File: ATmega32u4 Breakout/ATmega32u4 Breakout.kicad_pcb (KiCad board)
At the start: 2 copper layers, 6 parts, among them J1 Conn_01x22_Male, J2 Conn_01x22_Male, U1 ATmega32U4-AU, Y1 16MHz

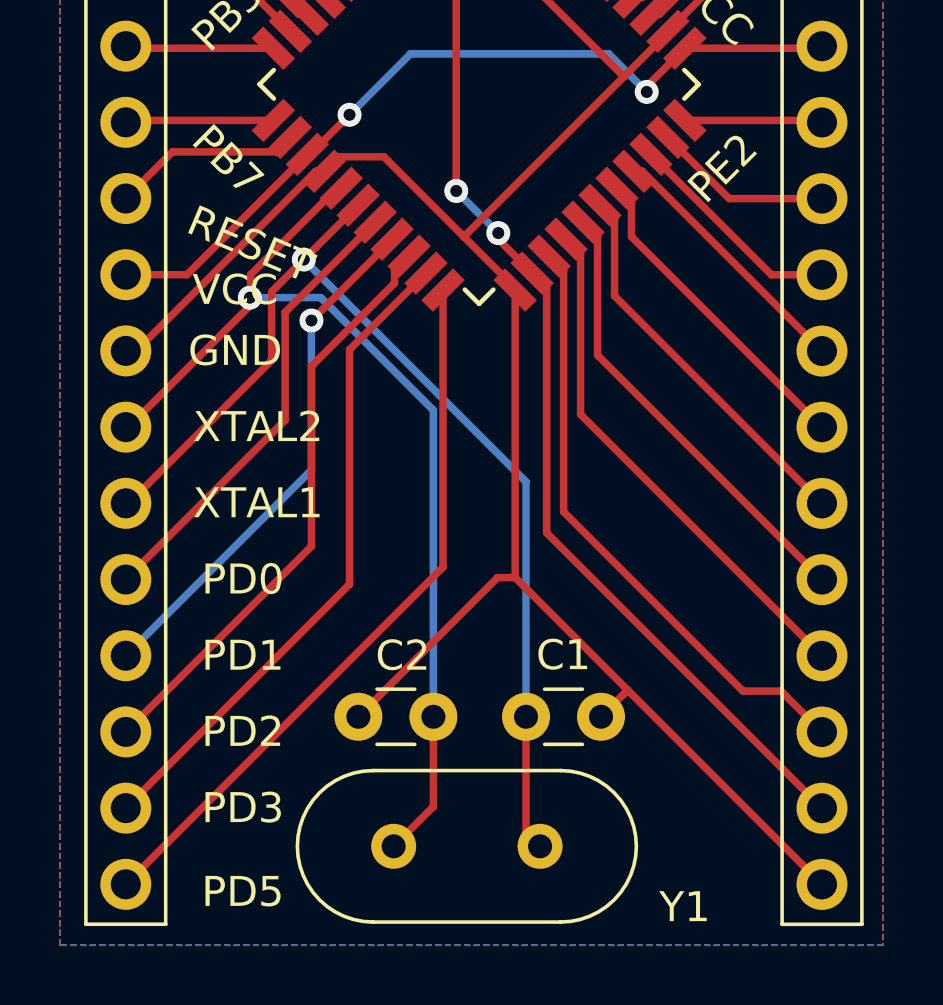
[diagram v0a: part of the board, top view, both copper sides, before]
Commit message: Moving labels around
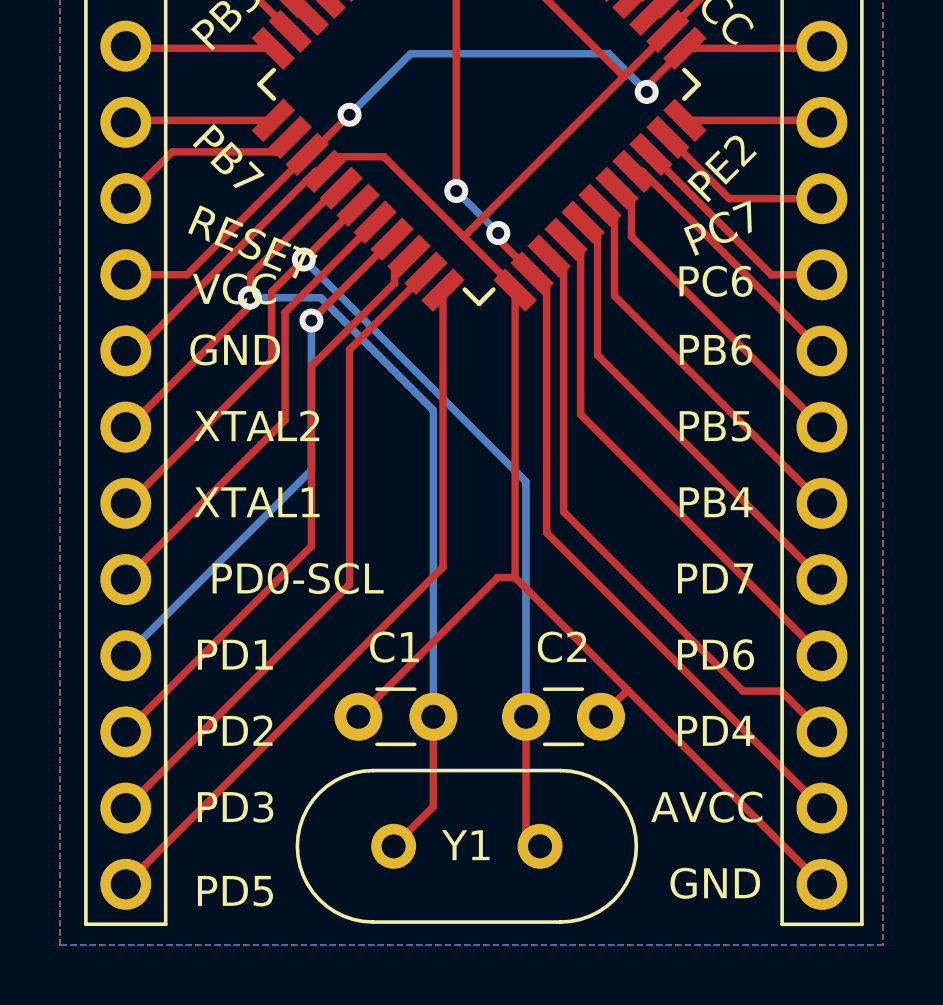
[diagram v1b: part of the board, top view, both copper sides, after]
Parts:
- moved C1 3.09 mm to (154.2, 110.0), turned to 180 degrees
- moved C2 3.09 mm to (157.3, 110.0), turned to 0 degrees
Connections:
- C1 pad 1: XTAL1 -> XTAL2
- C2 pad 1: XTAL2 -> XTAL1
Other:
- board text added: "PB4"
- board text added: "PB5"
- board text added: "PB6"
- board text added: "PC6"
- board text added: "PC7"
- board text added: "PD0-SCL"
- board text added: "PD4"
- board text added: "PD6"
- board text added: "PD7"
- board text removed: "PD0"
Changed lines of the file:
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@@
   (general
     (thickness 1.6)
-    (drawings 38)
+    (drawings 48)
     (tracks 180)
     (zones 0)
@@
   (page A4)
   (layers
-    (0 F.Cu signal)
+    (0 F.Cu signal hide)
     (31 B.Cu signal)
     (32 B.Adhes user)
@@
     (descr "C, Disc series, Radial, pin pitch=2.50mm, , diameter*width=3.0*1.6mm^2, Capacitor, http://www.vishay.com/docs/45233/krseries.pdf")
     (tags "C Disc series Radial pin pitch 2.50mm  diameter 3.0mm width 1.6mm Capacitor")
-    (fp_text reference C1 (at 1.25 -2.05) (layer F.SilkS)
-      (effects (font (size 1 1) (thickness 0.15)))
-    )
-    (fp_text value 22pF (at 5.548 0) (layer F.Fab)
+    (fp_text reference C2 (at 1.23 -2.286) (layer F.SilkS)
+      (effects (font (size 1 1) (thickness 0.15)))
+    )
+    (fp_text value 22pF (at 1.484 -2.286) (layer F.Fab)
       (effects (font (size 1 1) (thickness 0.15)))
     )
@@
     (descr "C, Disc series, Radial, pin pitch=2.50mm, , diameter*width=3.0*1.6mm^2, Capacitor, http://www.vishay.com/docs/45233/krseries.pdf")
     (tags "C Disc series Radial pin pitch 2.50mm  diameter 3.0mm width 1.6mm Capacitor")
-    (fp_text reference C2 (at 1.016 2.032) (layer F.SilkS)
-      (effects (font (size 1 1) (thickness 0.15)))
-    )
-    (fp_text value 22pF (at 5.588 0) (layer F.Fab)
+    (fp_text reference C1 (at 1.27 2.286) (layer F.SilkS)
+      (effects (font (size 1 1) (thickness 0.15)))
+    )
+    (fp_text value 22pF (at 1.016 2.286) (layer F.Fab)
       (effects (font (size 1 1) (thickness 0.15)))
     )
@@
     (descr "Crystal THT HC-49/U http://5hertz.com/pdfs/04404_D.pdf")
     (tags "THT crystalHC-49/U")
-    (fp_text reference Y1 (at -4.826 -2.032) (layer F.SilkS)
+    (fp_text reference Y1 (at 2.413 0) (layer F.SilkS)
       (effects (font (size 1 1) (thickness 0.15)))
     )
@@
     )
   )
+  (gr_text GND (at 163.576 115.57) (layer F.SilkS)
+    (effects (font (size 1 1) (thickness 0.15)))
+  )
+  (gr_text AVCC (at 163.322 113.03) (layer F.SilkS)
+    (effects (font (size 1 1) (thickness 0.15)))
+  )
+  (gr_text PD4 (at 163.576 110.49) (layer F.SilkS)
+    (effects (font (size 1 1) (thickness 0.15)))
+  )
+  (gr_text PD6 (at 163.576 107.95) (layer F.SilkS)
+    (effects (font (size 1 1) (thickness 0.15)))
+  )
+  (gr_text PD7 (at 163.576 105.41) (layer F.SilkS)
+    (effects (font (size 1 1) (thickness 0.15)))
+  )
+  (gr_text PB4 (at 163.576 102.87) (layer F.SilkS)
+    (effects (font (size 1 1) (thickness 0.15)))
+  )
+  (gr_text PB5 (at 163.576 100.33) (layer F.SilkS)
+    (effects (font (size 1 1) (thickness 0.15)))
+  )
+  (gr_text PB6 (at 163.576 97.79) (layer F.SilkS)
+    (effects (font (size 1 1) (thickness 0.15)))
+  )
+  (gr_text PC6 (at 163.576 95.504) (layer F.SilkS)
+    (effects (font (size 1 1) (thickness 0.15)))
+  )
+  (gr_text PC7 (at 163.83 93.726 23) (layer F.SilkS)
+    (effects (font (size 1 1) (thickness 0.15)))
+  )
   (gr_text PE2 (at 163.83 91.694 45) (layer F.SilkS)
     (effects (font (size 1 1) (thickness 0.15)))
@@
     (effects (font (size 1 1) (thickness 0.15)))
   )
-  (gr_text PD5 (at 147.828 115.824) (layer F.SilkS)
-    (effects (font (size 1 1) (thickness 0.15)))
-  )
-  (gr_text PD3 (at 147.828 113.03) (layer F.SilkS)
-    (effects (font (size 1 1) (thickness 0.15)))
-  )
-  (gr_text PD2 (at 147.828 110.49) (layer F.SilkS)
-    (effects (font (size 1 1) (thickness 0.15)))
-  )
-  (gr_text PD1 (at 147.828 107.95) (layer F.SilkS)
-    (effects (font (size 1 1) (thickness 0.15)))
-  )
-  (gr_text PD0 (at 147.828 105.41) (layer F.SilkS)
+  (gr_text PD5 (at 147.574 115.824) (layer F.SilkS)
+    (effects (font (size 1 1) (thickness 0.15)))
+  )
+  (gr_text PD3 (at 147.574 113.03) (layer F.SilkS)
+    (effects (font (size 1 1) (thickness 0.15)))
+  )
+  (gr_text PD2 (at 147.574 110.49) (layer F.SilkS)
+    (effects (font (size 1 1) (thickness 0.15)))
+  )
+  (gr_text PD1 (at 147.574 107.95) (layer F.SilkS)
+    (effects (font (size 1 1) (thickness 0.15)))
+  )
+  (gr_text PD0-SCL (at 149.606 105.41) (layer F.SilkS)
     (effects (font (size 1 1) (thickness 0.15)))
   )
@@
   (segment (start 160.528 88.646) (end 155.194 93.98) (width 0.25) (layer F.Cu) (net 15))
   (segment (start 161.99525 87.17875) (end 160.528 88.646) (width 0.25) (layer F.Cu) (net 15) (status 10))
-  (segment (start 159.766 109.982) (end 160.528 109.22) (width 0.25) (layer F.Cu) (net 15))
+  (segment (start 159.766 109.982) (end 160.528 109.22) (width 0.25) (layer F.Cu) (net 15) (status 10))
   (segment (start 160.528 109.22) (end 160.655 109.093) (width 0.25) (layer F.Cu) (net 15))
-  (segment (start 160.655 109.093) (end 167.132 115.57) (width 0.25) (layer F.Cu) (net 15))
+  (segment (start 160.655 109.093) (end 167.132 115.57) (width 0.25) (layer F.Cu) (net 15) (status 20))
   (segment (start 156.904082 105.342082) (end 160.655 109.093) (width 0.25) (layer F.Cu) (net 15))
   (segment (start 156.317918 105.342082) (end 156.904082 105.342082) (width 0.25) (layer F.Cu) (net 15))
-  (segment (start 151.678 109.982) (end 156.317918 105.342082) (width 0.25) (layer F.Cu) (net 15))
+  (segment (start 151.678 109.982) (end 156.317918 105.342082) (width 0.25) (layer F.Cu) (net 15) (status 10))
   (segment (start 150.851806 92.480194) (end 148.082 95.25) (width 0.25) (layer F.Cu) (net 16) (status 10))
   (segment (start 148.082 95.25) (end 148.082 96.127371) (width 0.25) (layer F.Cu) (net 16))
   (segment (start 144.020999 100.327001) (end 143.925001 100.327001) (width 0.25) (layer F.Cu) (net 16) (status 30))
   (segment (start 148.336 96.012) (end 144.020999 100.327001) (width 0.25) (layer F.Cu) (net 16) (status 20))
-  (segment (start 154.178 112.976) (end 152.854 114.3) (width 0.25) (layer F.Cu) (net 16))
-  (segment (start 154.178 109.982) (end 154.178 112.976) (width 0.25) (layer F.Cu) (net 16))
+  (segment (start 154.178 112.976) (end 152.854 114.3) (width 0.25) (layer F.Cu) (net 16) (status 20))
+  (segment (start 154.178 109.982) (end 154.178 112.976) (width 0.25) (layer F.Cu) (net 16) (status 10))
   (via (at 148.06101 96.012) (size 0.8) (drill 0.4) (layers F.Cu B.Cu) (net 16))
   (segment (start 150.425002 96.012) (end 148.06101 96.012) (width 0.25) (layer B.Cu) (net 16))
   (segment (start 154.178 99.764998) (end 150.425002 96.012) (width 0.25) (layer B.Cu) (net 16))
-  (segment (start 154.178 109.982) (end 154.178 99.764998) (width 0.25) (layer B.Cu) (net 16))
+  (segment (start 154.178 109.982) (end 154.178 99.764998) (width 0.25) (layer B.Cu) (net 16) (status 10))
   (segment (start 148.78601 95.81599) (end 148.78601 98.10199) (width 0.25) (layer F.Cu) (net 17))
   (segment (start 144.020999 102.867001) (end 143.925001 102.867001) (width 0.25) (layer F.Cu) (net 17) (status 30))
   (segment (start 148.78601 98.10199) (end 144.020999 102.867001) (width 0.25) (layer F.Cu) (net 17) (status 20))
-  (segment (start 157.266 113.832) (end 157.734 114.3) (width 0.25) (layer F.Cu) (net 17))
-  (segment (start 157.266 109.982) (end 157.266 113.832) (width 0.25) (layer F.Cu) (net 17))
-  (via (at 157.266 109.982) (size 0.8) (drill 0.4) (layers F.Cu B.Cu) (net 17))
+  (segment (start 157.266 113.832) (end 157.734 114.3) (width 0.25) (layer F.Cu) (net 17) (status 30))
+  (segment (start 157.266 109.982) (end 157.266 113.832) (width 0.25) (layer F.Cu) (net 17) (status 30))
+  (via (at 157.266 109.982) (size 0.8) (drill 0.4) (layers F.Cu B.Cu) (net 17) (status 30))
   (segment (start 157.266 102.148) (end 149.86 94.742) (width 0.25) (layer B.Cu) (net 17))
   (via (at 149.86 94.742) (size 0.8) (drill 0.4) (layers F.Cu B.Cu) (net 17))
-  (segment (start 157.266 109.982) (end 157.266 102.148) (width 0.25) (layer B.Cu) (net 17))
+  (segment (start 157.266 109.982) (end 157.266 102.148) (width 0.25) (layer B.Cu) (net 17) (status 10))
   (segment (start 149.86 94.742) (end 148.78601 95.81599) (width 0.25) (layer F.Cu) (net 17))
-  (segment (start 151.671491 92.930509) (end 149.86 94.742) (width 0.25) (layer F.Cu) (net 17))
+  (segment (start 151.671491 92.930509) (end 149.86 94.742) (width 0.25) (layer F.Cu) (net 17) (status 10))
   (segment (start 149.236019 100.095983) (end 143.925001 105.407001) (width 0.25) (layer F.Cu) (net 18) (status 20))
   (segment (start 149.236019 96.497352) (end 149.236019 100.095983) (width 0.25) (layer F.Cu) (net 18))
@@
   (segment (start 159.944643 84.869491) (end 161.777067 83.037067) (width 0.25) (layer F.Cu) (net 35) (status 10))
   (segment (start 159.732509 84.869491) (end 159.944643 84.869491) (width 0.25) (layer F.Cu) (net 35) (status 30))
-  (segment (start 161.777067 80.284933) (end 167.132 74.93) (width 0.25) (layer F.Cu) (net 35))
+  (segment (start 161.777067 80.284933) (end 167.132 74.93) (width 0.25) (layer F.Cu) (net 35) (status 20))
   (segment (start 161.777067 83.037067) (end 161.777067 80.284933) (width 0.25) (layer F.Cu) (net 35))
   (segment (start 159.166823 84.303806) (end 161.036 82.434629) (width 0.25) (layer F.Cu) (net 36) (status 10))

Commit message: Lots of work over the weekend.
Nearly done, gerber files made too.  I think it's ready to be turned into PCB.
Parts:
- moved J2 17.4 mm to (152.1, 71.1)
- moved U1 16.3 mm to (142.0, 97.8)
- moved Y1 16.1 mm to (142.0, 117.6), turned to 270 degrees
- moved J1 15.0 mm to (131.8, 71.1)
- moved C2 14.3 mm to (143.3, 112.8), turned to 90 degrees
- moved C1 13.5 mm to (140.7, 110.2), turned to 270 degrees
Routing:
- net GND: track 95.5 -> 76.7 mm
- net XTAL1: track 36.0 -> 31.4 mm, vias 2 -> 1
- net VCC: track 27.5 -> 23.5 mm
- net PB1: track 7.71 -> 5.97 mm
- net PB3: track 4.95 -> 3.33 mm
- net PB7: track 4.94 -> 3.33 mm
- net PE2: track 4.60 -> 3.08 mm
- net PB2: track 6.33 -> 4.97 mm
- net PD4: track 20.4 -> 19.1 mm
- net PC7: track 5.98 -> 4.71 mm
- net PC6: track 7.37 -> 6.10 mm
- net PF4: track 13.8 -> 12.6 mm
- net PF7: track 7.37 -> 6.26 mm
- net PB0: track 9.10 -> 8.06 mm
- net AREF: track 20.1 -> 19.1 mm
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- removed copper zone on F.Cu, net GND
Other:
- board outline added: 24.4 x 57.4 mm
- net class Power added: clearance 0.2, trace_width 0.4, via_dia 0.7, via_drill 0.5
- rule pad_to_mask_clearance: 0 -> 0.0508
- board text added: "ATmega32u4"
- board text added: "PB0-SS"
- board text added: "PB1-SCLK"
- board text added: "PB2-MOSI"
- board text added: "PB3-MISO"
- board text added: "PB4-A11"
- board text added: "PB5-A12"
- board text added: "PB6-A10"
- board text added: "PD1-SDA"
- board text added: "PD2-RXD"
- board text added: "PD3-TXD"
- board text added: "PD6-T1"
- board text added: "PD7-T0"
- board text added: "PE6-D7"
- board text added: "PF0-A0"
- board text added: "PF1-A1"
- board text added: "PF4-A4"
- board text added: "PF5-A5"
- board text added: "PF6-A6"
- board text added: "PF7-A7"
- board text added: "RES"
- board text added: "SRT0001"
- board text removed: "D7"
- board text removed: "PB0"
- board text removed: "PB1"
- board text removed: "PB2"
- board text removed: "PB3"
- board text removed: "PB4"
- board text removed: "PB5"
- board text removed: "PB6"
- board text removed: "PD1"
- board text removed: "PD2"
- board text removed: "PD3"
- board text removed: "PD6"
- board text removed: "PD7"
- board text removed: "PF0"
- board text removed: "PF1"
- board text removed: "PF4"
- board text removed: "PF5"
- board text removed: "PF6"
- board text removed: "PF7"
- board text removed: "RESET"
